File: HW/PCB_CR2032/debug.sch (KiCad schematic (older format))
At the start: 2 parts, among them J1 DBG

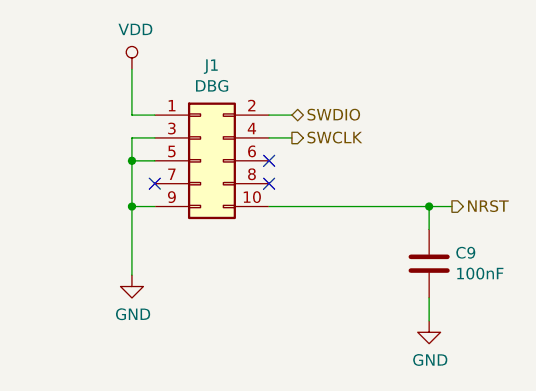
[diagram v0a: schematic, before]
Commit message: * Updated Schematic with 1206 leds and 1k 0805 current limiting resistors
* Restored STDC14 and debug UART, now shared with top led of minute and second. Some other LED pins remapped

* Updated STM32CubeMX project to reflect schematic changes and generated code again
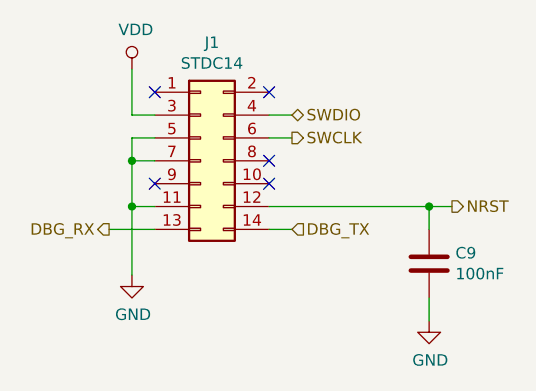
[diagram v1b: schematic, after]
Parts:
- removed J1: DBG, Connector_PinHeader_1.27mm:PinHeader_2x05_P1.27mm_Vertical_SMD, symbol Connector_Generic:Conn_02x05_Odd_Even
- added J1: STDC14, Connector_PinHeader_1.27mm:PinHeader_2x07_P1.27mm_Vertical_SMD, symbol Connector_Generic:Conn_02x07_Odd_Even
- C9: Make (none) -> Yageo; Mouser (none) -> 603-CC805KRX7R9BB104; Part (none) -> CC0805KRX7R9BB104
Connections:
- net GND: now also J1.11 (Pin_11), J1.5 (Pin_5), J1.7 (Pin_7)
- net NRST: now also J1.12 (Pin_12)
- net SWCLK: now also J1.6 (Pin_6)
- net SWDIO: now also J1.4 (Pin_4)
- net VDD: now also J1.3 (Pin_3)
- new net DBG_RX: J1.13 (Pin_13)
- new net DBG_TX: J1.14 (Pin_14)
- no-connect marks 3 -> 5
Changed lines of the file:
@@
 F 2 "Capacitor_SMD:C_0805_2012Metric_Pad1.15x1.40mm_HandSolder" H 6738 4000 50  0001 C CNN
 F 3 "~" H 6700 4150 50  0001 C CNN
+F 4 "Yageo" H 6700 4150 50  0001 C CNN "Make"
+F 5 "603-CC805KRX7R9BB104" H 6700 4150 50  0001 C CNN "Mouser"
+F 6 "CC0805KRX7R9BB104" H 6700 4150 50  0001 C CNN "Part"
 	1    6700 4150
 	1    0    0    -1
@@
 NoConn ~ 6000 3800
 $Comp
-L Connector_Generic:Conn_02x05_Odd_Even J1
-U 1 1 5DC80BC0
+L Connector_Generic:Conn_02x07_Odd_Even J1
+U 1 1 5DC60481
 P 5700 3700
-F 0 "J1" H 5750 4117 50  0000 C CNN
-F 1 "DBG" H 5750 4026 50  0000 C CNN
-F 2 "Connector_PinHeader_1.27mm:PinHeader_2x05_P1.27mm_Vertical_SMD" H 5700 3700 50  0001 C CNN
+F 0 "J1" H 5750 4217 50  0000 C CNN
+F 1 "STDC14" H 5750 4126 50  0000 C CNN
+F 2 "Connector_PinHeader_1.27mm:PinHeader_2x07_P1.27mm_Vertical_SMD" H 5700 3700 50  0001 C CNN
 F 3 "~" H 5700 3700 50  0001 C CNN
+F 4 "Amphenol" H 5700 3700 50  0001 C CNN "Make"
+F 5 "649-221121-00014T4LF" H 5700 3700 50  0001 C CNN "Mouser"
+F 6 "20021121-00014T4LF" H 5700 3700 50  0001 C CNN "Part"
 	1    5700 3700
 	1    0    0    -1
 $EndComp
+Text HLabel 5300 4000 0    50   Output ~ 0
+DBG_RX
+Wire Wire Line
+	5300 4000 5500 4000
+Text HLabel 6100 4000 2    50   Input ~ 0
+DBG_TX
+Wire Wire Line
+	6100 4000 6000 4000
+NoConn ~ 5500 3400
+NoConn ~ 6000 3400
 $EndSCHEMATC

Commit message: Created layout for CR2032 version 1.0, for first prototype order, resulted in a lot of changes in the pin-mapping to make routing easier.
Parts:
- C9: footprint Capacitor_SMD:C_0805_2012Metric_Pad1.15x1.40mm_HandSolder -> Capacitor_SMD:C_0603_1608Metric_Pad1.05x0.95mm_HandSolder; LCSC (none) -> C14663; Make Yageo -> (none); Mouser 603-CC805KRX7R9BB104 -> (none); Part CC0805KRX7R9BB104 -> (none); jlcpcb (none) -> CC0603KRX7R9BB104
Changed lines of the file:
@@
 F 0 "C9" H 6815 4196 50  0000 L CNN
 F 1 "100nF" H 6815 4105 50  0000 L CNN
-F 2 "Capacitor_SMD:C_0805_2012Metric_Pad1.15x1.40mm_HandSolder" H 6738 4000 50  0001 C CNN
+F 2 "Capacitor_SMD:C_0603_1608Metric_Pad1.05x0.95mm_HandSolder" H 6738 4000 50  0001 C CNN
 F 3 "~" H 6700 4150 50  0001 C CNN
-F 4 "Yageo" H 6700 4150 50  0001 C CNN "Make"
-F 5 "603-CC805KRX7R9BB104" H 6700 4150 50  0001 C CNN "Mouser"
-F 6 "CC0805KRX7R9BB104" H 6700 4150 50  0001 C CNN "Part"
+F 4 "" H 6700 4150 50  0001 C CNN "Make"
+F 5 "" H 6700 4150 50  0001 C CNN "Mouser"
+F 6 "" H 6700 4150 50  0001 C CNN "Part"
+F 7 "CC0603KRX7R9BB104" H 6700 4150 50  0001 C CNN "jlcpcb"
+F 8 "C14663" H 6700 4150 50  0001 C CNN "LCSC"
 	1    6700 4150
 	1    0    0    -1
